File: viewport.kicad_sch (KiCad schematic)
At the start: 11 parts, among them U11 74LS00, U12 74LS30, U13 74LS20, U14 74LS14, U15 74LS30, U16 74LS20, U17 74LS30, U18 74LS00, U19 74LS32, U20 74LS30, U9 74LS32

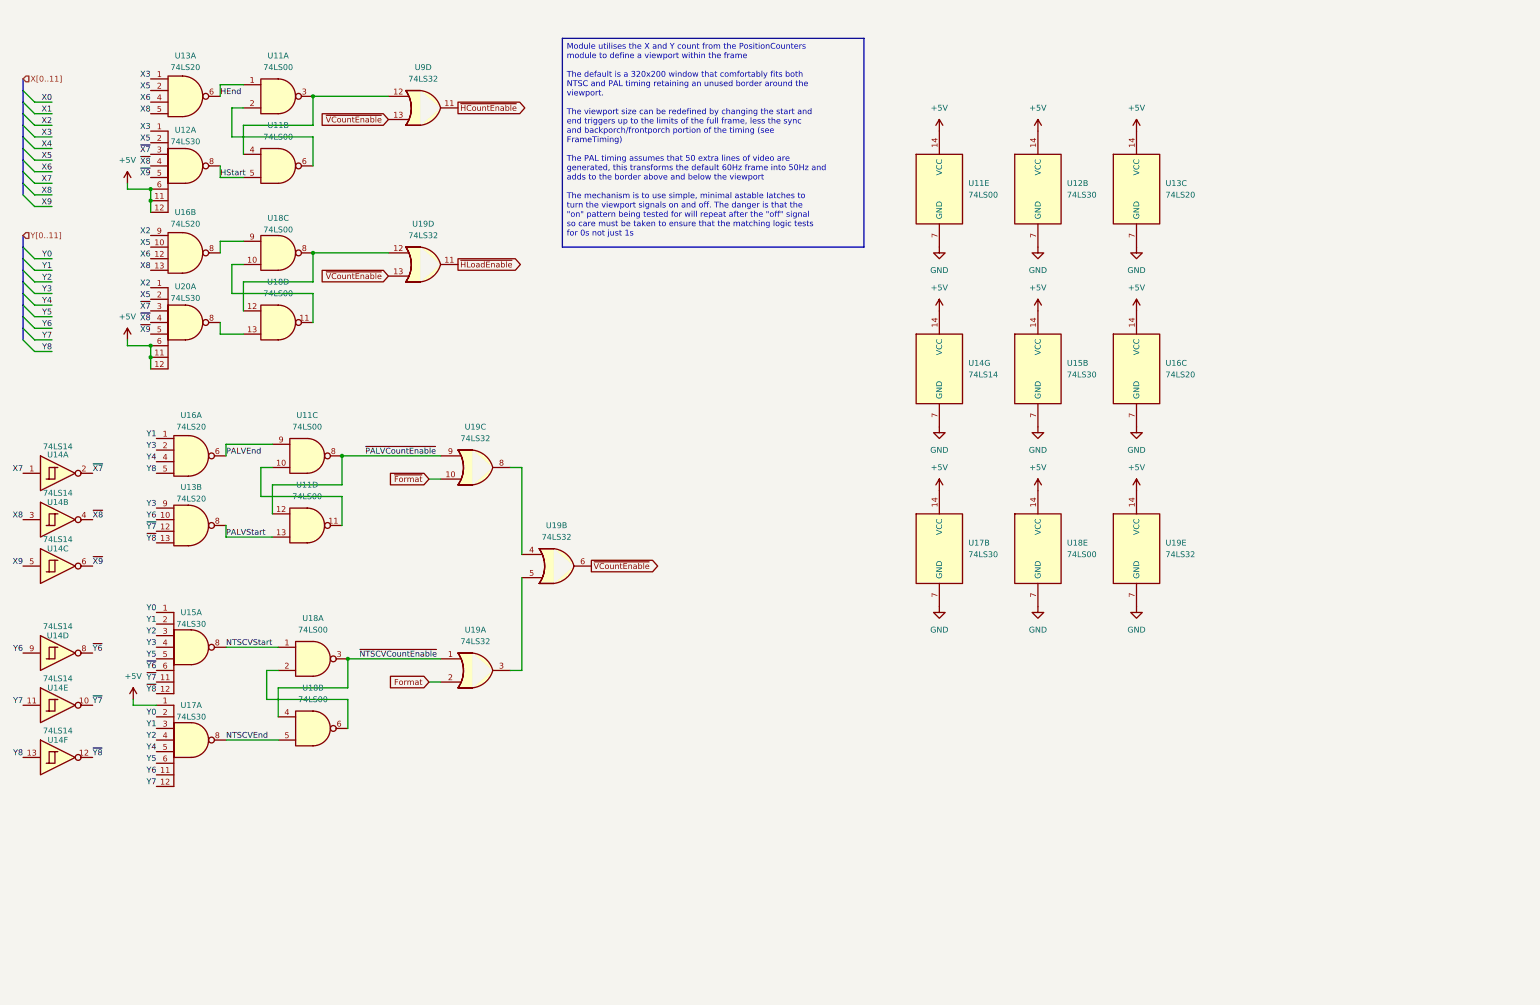
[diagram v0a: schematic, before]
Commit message: revise position counter
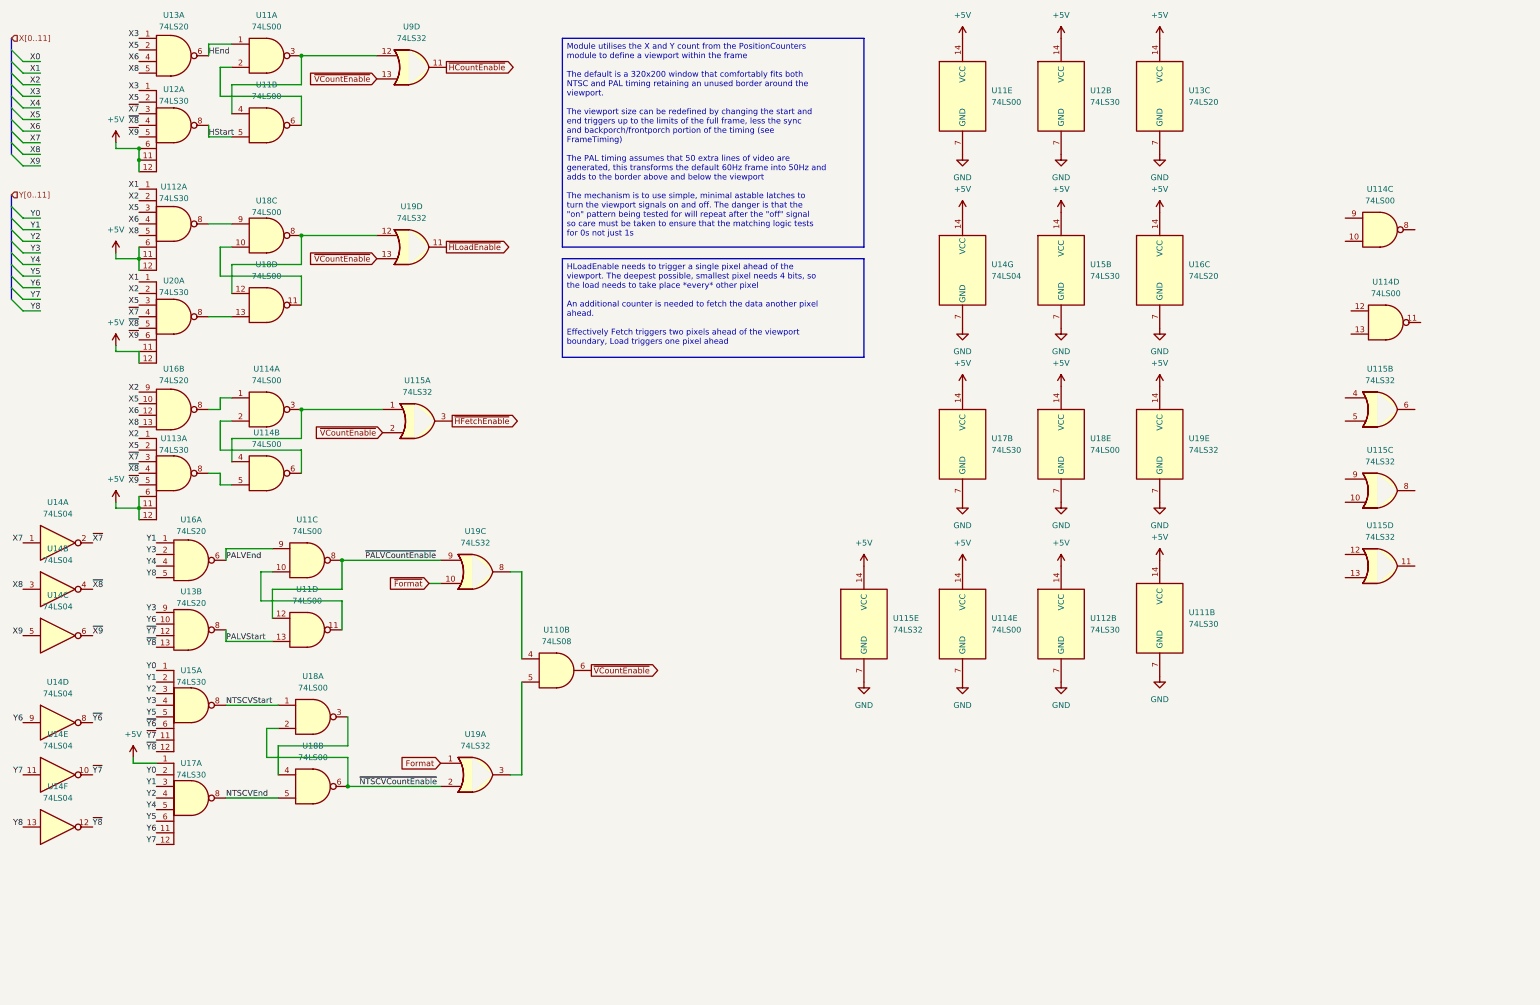
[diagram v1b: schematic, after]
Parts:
- removed U14: 74LS14, Package_SO:SO-14_3.9x8.65mm_P1.27mm, symbol 74xx:74LS14
- removed unit 2 of U19
- added U110: 74LS08, symbol 74xx:74LS08
- added U111, U112, U113: 74LS30, symbol 74xx:74LS30
- added U114: 74LS00, symbol 74xx:74LS00
- added U115: 74LS32, symbol 74xx:74LS32
- added U14: 74LS04, Package_SO:SO-14_3.9x8.65mm_P1.27mm, symbol 74xx:74LS04
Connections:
- net +5V: now also U111.14 (VCC), U112.11, U112.12, U112.14 (VCC), U112.6, U113.11, U113.12, U113.6, U114.14 (VCC), U115.14 (VCC), U14.14 (VCC); no longer U20.6
- net Format: now also U19.1; no longer U19.2
- net GND: now also U111.7 (GND), U112.7 (GND), U114.7 (GND), U115.7 (GND), U14.7 (GND)
- net X1: now also U20.1, U112.1
- net X2: now also U20.2, U112.2, U113.1; no longer U20.1
- net X5: now also U20.3, U112.3, U113.2; no longer U20.2
- net X6: now also U112.4
- net X7: now also U14.1
- net X8: now also U112.5, U14.3
- net X9: now also U14.5
- net Y6: now also U14.9
- net Y7: now also U14.11
- net Y8: now also U14.13
- net ~{NTSCVCountEnable}: now also U18.2, U18.6, U19.2; no longer U18.3, U18.4, U19.1
- net ~{VCountEnable}: now also U110.6, U115.2
- net ~{X7}: now also U20.4, U113.3, U14.2; no longer U20.3
- net ~{X8}: now also U20.5, U113.4, U14.4; no longer U20.4
- net ~{X9}: now also U20.6, U113.5, U14.6; no longer U20.5
- net ~{Y6}: now also U14.8
- net ~{Y7}: now also U14.10
- net ~{Y8}: now also U14.12
- net at U19.8: now also U110.4
- net at U19.3: now also U110.5
- net at U16.8: now also U114.1; no longer U18.9
- new net: U18.3, U18.4
- new net: U114.2, U114.6
- new net: U114.3, U114.4, U115.1
- new net: U112.8, U18.9
- new net: U113.8, U114.5
- new net ~{HFetchEnable}: U115.3
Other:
- moved on the sheet: U11A, U11B, U11C, U11D, U11E, U12A, U12B, U13A, U13B, U13C, U15A, U15B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

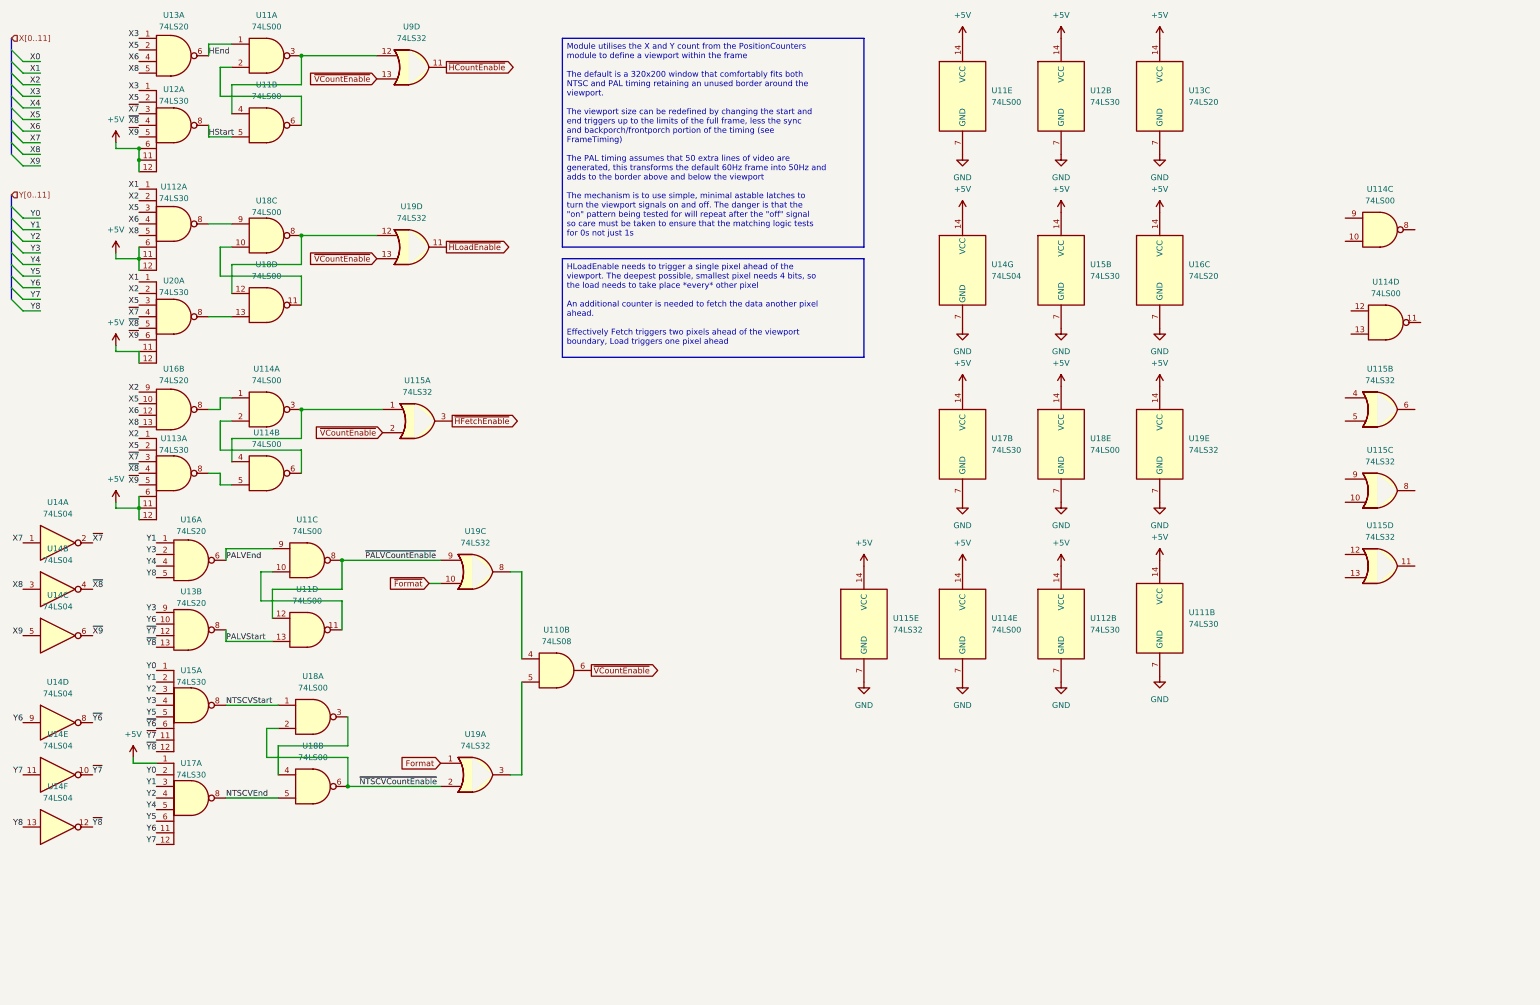
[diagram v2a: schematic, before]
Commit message: isolate each schematic function for testing
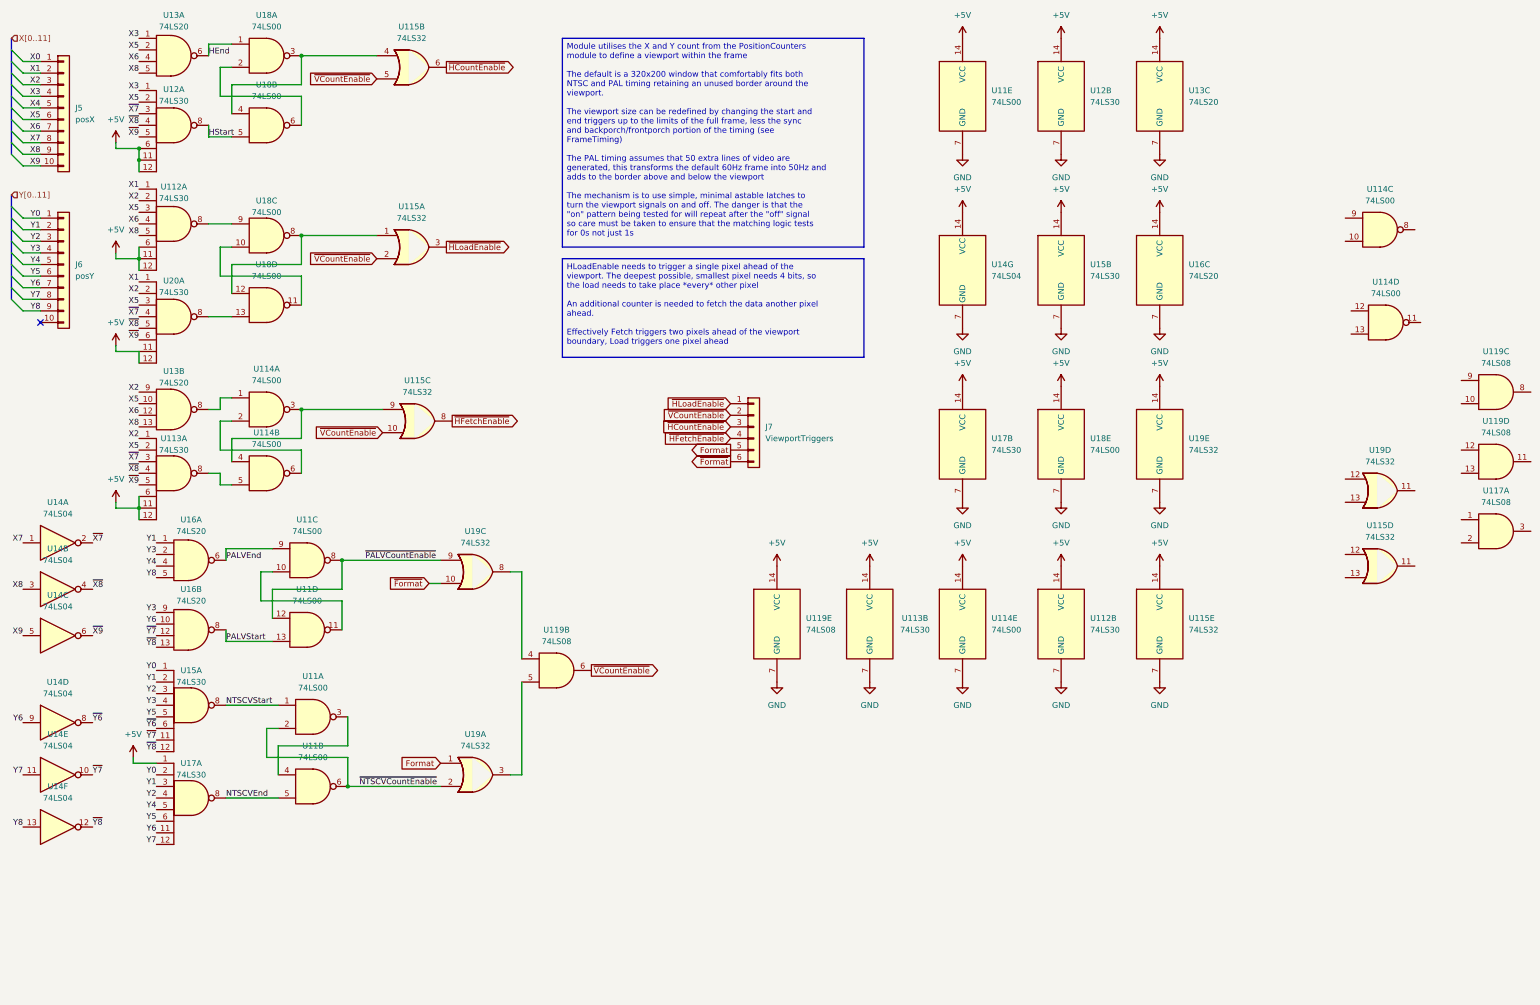
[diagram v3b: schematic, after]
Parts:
- removed U110: 74LS08, symbol 74xx:74LS08
- removed U111: 74LS30, symbol 74xx:74LS30
- removed U9: 74LS32, Package_SO:SO-14_3.9x8.65mm_P1.27mm, symbol 74xx:74LS32
- added J5: posX, Connector_PinSocket_2.54mm:PinSocket_1x10_P2.54mm_Vertical, symbol Connector_Generic:Conn_01x10
- added J6: posY, Connector_PinSocket_2.54mm:PinSocket_1x10_P2.54mm_Vertical, symbol Connector_Generic:Conn_01x10
- added J7: ViewportTriggers, Connector_PinSocket_2.54mm:PinSocket_1x06_P2.54mm_Vertical, symbol Connector_Generic:Conn_01x06
- added unit 2 of U113
- added U117: 74LS08, symbol 74xx:74LS08
- added U119: 74LS08, Package_SO:SOIC-14_3.9x8.7mm_P1.27mm, symbol 74xx:74LS08
- U112, U113, U114, U115: footprint (none) -> Package_SO:SO-14_3.9x8.65mm_P1.27mm
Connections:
- net +5V: now also U113.14 (VCC), U119.14 (VCC)
- net Format: now also J7.5 (Pin_5)
- net GND: now also U113.7 (GND), U119.7 (GND)
- net HEnd: now also U18.1; no longer U11.1
- net HStart: now also U18.5; no longer U11.5
- net NTSCVEnd: now also U11.5; no longer U18.5
- net NTSCVStart: now also U11.1; no longer U18.1
- net PALVStart: now also U16.8; no longer U13.8
- net X0: now also J5.1 (Pin_1)
- net X1: now also J5.2 (Pin_2)
- net X2: now also U13.9, J5.3 (Pin_3); no longer U16.9
- net X3: now also J5.4 (Pin_4)
- net X4: now also J5.5 (Pin_5)
- net X5: now also U13.10, J5.6 (Pin_6); no longer U16.10
- net X6: now also U13.12, J5.7 (Pin_7); no longer U16.12
- net X7: now also J5.8 (Pin_8)
- net X8: now also U13.13, J5.9 (Pin_9); no longer U16.13
- net X9: now also J5.10 (Pin_10)
- net Y0: now also J6.1 (Pin_1)
- net Y1: now also J6.2 (Pin_2)
- net Y2: now also J6.3 (Pin_3)
- net Y3: now also U16.9, J6.4 (Pin_4); no longer U13.9
- net Y4: now also J6.5 (Pin_5)
- net Y5: now also J6.6 (Pin_6)
- net Y6: now also U16.10, J6.7 (Pin_7); no longer U13.10
- net Y7: now also J6.8 (Pin_8)
- net Y8: now also J6.9 (Pin_9)
- net ~{Format}: now also J7.6 (Pin_6)
- net ~{HCountEnable}: now also U115.6, J7.3 (Pin_3)
- net ~{HFetchEnable}: now also U115.8, J7.4 (Pin_4); no longer U115.3
- net ~{HLoadEnable}: now also U115.3, J7.1 (Pin_1); no longer U19.11
- net ~{NTSCVCountEnable}: now also U11.2, U11.6; no longer U18.2, U18.6
- net ~{VCountEnable}: now also U115.10, U115.5, J7.2 (Pin_2), U119.6; no longer U19.13
- net ~{Y7}: now also U16.12; no longer U13.12
- net ~{Y8}: now also U16.13; no longer U13.13
- net at U18.3, U18.4: now also U115.4
- net at U114.1: now also U13.8; no longer U16.8
- net at U114.3, U114.4: now also U115.9; no longer U115.1
- net at U19.3: now also U119.5
- net at U18.12, U18.8: now also U115.1; no longer U19.12
- net at U19.8: now also U119.4
- new net: U18.2, U18.6
- no-connect marks 0 -> 1
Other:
- moved on the sheet: U115B, U115C, U115E

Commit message: rework schematic isolation
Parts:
- added unit 2 of U20
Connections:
- net +5V: now also U20.14 (VCC)
- net GND: now also U20.7 (GND)
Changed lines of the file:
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@@
+	)
+	(symbol
+		(lib_id "power:GND")
+		(at 204.47 120.65 0)
+		(unit 1)
+		(exclude_from_sim no)
+		(in_bom yes)
+		(on_board yes)
+		(dnp no)
+		(fields_autoplaced yes)
+		(property "Reference" "#PWR0237"
+			(at 204.47 127 0)
+			(effects
+				(font
+					(size 1.27 1.27)
+				)
+				(hide yes)
+			)
+		)
+		(property "Value" "GND"
+			(at 204.47 125.73 0)
+			(effects
+				(font
+					(size 1.27 1.27)
+				)
+			)
+		)
+		(property "Footprint" ""
+			(at 204.47 120.65 0)
+			(effects
+				(font
+					(size 1.27 1.27)
+				)
+				(hide yes)
+			)
+		)
+		(property "Datasheet" ""
+			(at 204.47 120.65 0)
+			(effects
+				(font
+					(size 1.27 1.27)
+				)
+				(hide yes)
+			)
+		)
+		(property "Description" "Power symbol creates a global label with name \"GND\" , ground"
+			(at 204.47 120.65 0)
+			(effects
+				(font
+					(size 1.27 1.27)
+				)
+				(hide yes)
+			)
+		)
+		(pin "1"
+		)
+		(instances
+			(project "DIY-Video"
+				(path "/6c4ef05c-ecf5-4bee-ae4e-d72f13738678/4023660c-3ec4-409a-be3a-58018e7d8eb1"
+					(reference "#PWR0237")
+					(unit 1)
+				)
+			)
+		)
 	)
 	(symbol
@@
 	(symbol
 		(lib_id "74xx:74LS30")
+		(at 204.47 107.95 0)
+		(unit 2)
+		(exclude_from_sim no)
+		(in_bom yes)
+		(on_board yes)
+		(dnp no)
+		(fields_autoplaced yes)
+		(property "Reference" "U20"
+			(at 210.82 106.6799 0)
+			(effects
+				(font
+					(size 1.27 1.27)
+				)
+				(justify left)
+			)
+		)
+		(property "Value" "74LS30"
+			(at 210.82 109.2199 0)
+			(effects
+				(font
+					(size 1.27 1.27)
+				)
+				(justify left)
+			)
+		)
+		(property "Footprint" "Package_SO:SO-14_3.9x8.65mm_P1.27mm"
+			(at 204.47 107.95 0)
+			(effects
+				(font
+					(size 1.27 1.27)
+				)
+				(hide yes)
+			)
+		)
+		(property "Datasheet" "http://www.ti.com/lit/gpn/sn74LS30"
+			(at 204.47 107.95 0)
+			(effects
+				(font
+					(size 1.27 1.27)
+				)
+				(hide yes)
+			)
+		)
+		(property "Description" "8-input NAND"
+			(at 204.47 107.95 0)
+			(effects
+				(font
+					(size 1.27 1.27)
+				)
+				(hide yes)
+			)
+		)
+		(pin "1"
+		)
+		(pin "3"
+		)
+		(pin "5"
+		)
+		(pin "4"
+		)
+		(pin "6"
+		)
+		(pin "11"
+		)
+		(pin "2"
+		)
+		(pin "12"
+		)
+		(pin "8"
+		)
+		(pin "7"
+		)
+		(pin "14"
+		)
+		(instances
+			(project "DIY-Video"
+				(path "/6c4ef05c-ecf5-4bee-ae4e-d72f13738678/4023660c-3ec4-409a-be3a-58018e7d8eb1"
+					(reference "U20")
+					(unit 2)
+				)
+			)
+		)
+	)
+	(symbol
+		(lib_id "74xx:74LS30")
 		(at 55.88 165.1 0)
 		(unit 1)
@@
 				)
 			)
+		)
+	)
+	(symbol
+		(lib_id "power:+5V")
+		(at 204.47 95.25 0)
+		(unit 1)
+		(exclude_from_sim no)
+		(in_bom yes)
+		(on_board yes)
+		(dnp no)
+		(fields_autoplaced yes)
+		(property "Reference" "#PWR0236"
+			(at 204.47 99.06 0)
+			(effects
+				(font
+					(size 1.27 1.27)
+				)
+				(hide yes)
+			)
+		)
+		(property "Value" "+5V"
+			(at 204.47 90.17 0)
+			(effects
+				(font
+					(size 1.27 1.27)
+				)
+			)
+		)
+		(property "Footprint" ""
+			(at 204.47 95.25 0)
+			(effects
+				(font
+					(size 1.27 1.27)
+				)
+				(hide yes)
+			)
+		)
+		(property "Datasheet" ""
+			(at 204.47 95.25 0)
+			(effects
+				(font
+					(size 1.27 1.27)
+				)
+				(hide yes)
+			)
+		)
+		(property "Description" "Power symbol creates a global label with name \"+5V\""
+			(at 204.47 95.25 0)
+			(effects
+				(font
+					(size 1.27 1.27)
+				)
+				(hide yes)
+			)
+		)
+		(pin "1"
+		)
+		(instances
+			(project "DIY-Video"
+				(path "/6c4ef05c-ecf5-4bee-ae4e-d72f13738678/4023660c-3ec4-409a-be3a-58018e7d8eb1"
+					(reference "#PWR0236")
+					(unit 1)
+				)
+			)

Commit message: spin register out as separate board
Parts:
- U117: footprint (none) -> Package_SO:SO-14_3.9x8.65mm_P1.27mm
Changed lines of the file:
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@@
 			)
 		)
-		(property "Footprint" ""
+		(property "Footprint" "Package_SO:SO-14_3.9x8.65mm_P1.27mm"
 			(at 341.63 127 0)
 			(effects

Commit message: refine main board layout
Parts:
- added C13, C14, C15, C16, C17, C18, C19, C20, C21, C22, C23, C24, C25, C26, C27: 10nF, Capacitor_SMD:C_0603_1608Metric, symbol Device:C_Small
- added J43: Power, Connector_PinSocket_2.54mm:PinSocket_1x04_P2.54mm_Vertical, symbol Connector_Generic:Conn_01x04
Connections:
- net +5V: now also C13.1, C14.1, C15.1, C16.1, C17.1, C18.1, C19.1, C20.1, C21.1, C22.1, C23.1, C24.1, C25.1, C26.1, C27.1, J43.1 (Pin_1), J43.4 (Pin_4)
- net GND: now also C13.2, C14.2, C15.2, C16.2, C17.2, C18.2, C19.2, C20.2, C21.2, C22.2, C23.2, C24.2, C25.2, C26.2, C27.2, J43.2 (Pin_2), J43.3 (Pin_3)
